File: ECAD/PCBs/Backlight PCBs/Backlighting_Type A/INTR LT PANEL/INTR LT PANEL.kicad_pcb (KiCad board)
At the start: 2 copper layers, 138.9 x 83.9 mm, 90 parts, among them J1 Conn_01x04_Female, J2 Conn_01x04_Female

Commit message: Drawing Sheet & Silkscreen update - Backlight Panels (Fc thru Spin)
1:  Updated/Relinked Drawing Sheet for both PCB and Schematics
2:  Standardized Silkscreen (if required)

Finished Remaining Backlighting Type A & Type B PCBs.....
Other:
- board text added: "INTR LT PANEL Revision: 3 www.openhornet.com"
- board text removed: "INTR LT PANEL Version 2.2 www.openhornet.com"
- board text removed: "Version 2.0"
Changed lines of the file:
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@@
   )
   (paper "A4")
+  (title_block
+    (title "INTR LT PANEL")
+    (date "2023-02-10")
+    (rev "3")
+  )
   (layers
     (0 "F.Cu" signal)
@@
     (effects (font (size 1 1) (thickness 0.15)) (justify mirror))
   )
-  (gr_text "INTR LT PANEL\nVersion 2.2\nwww.openhornet.com" (at 59.944 75.692) (layer "B.SilkS")
+  (gr_text "INTR LT PANEL\nRevision: 3\nwww.openhornet.com" (at 59.944 75.692) (layer "B.SilkS")
     (effects (font (size 1 1) (thickness 0.15)) (justify mirror))
   )
@@
     (effects (font (size 1 1) (thickness 0.15)) (justify mirror))
   )
-  (gr_text "Version 2.0" (at 157.375 81.55) (layer "B.SilkS")
-    (effects (font (size 1 1) (thickness 0.15)) (justify mirror))
-  )

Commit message: Review: HUD VID RCD thru INTR LT 100%
Reviewed/adjusted silkscreens as needed
Relinked footprints
Updated Manufacturing files
Updated PNGs and STEP files as needed.
Renamed PNGs for standardization
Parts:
- 1, 10, 11, 6: footprint OH_Backlighting:OH_Panel_6-32_PHS -> OH_Footprints:OH_Panel_6-32_PHS
- 2: footprint OH_Backlighting:SxAL_Toggle_13x13mm -> OH_Footprints:SxAL_Toggle_13x13mm
- 3, 4, 7, 8, 9: footprint OH_Backlighting:BR10K_Pot_11mm_x_11mm -> OH_Footprints:BR10K_Pot_11mm_x_11mm
- 5: footprint OH_Backlighting:631H_Toggle_13mm_x_13mm -> OH_Footprints:631H_Toggle_13mm_x_13mm
- G1: footprint Kicad Footprint Files:631HToggle -> OH_Footprints:631H_Toggle_Silkscreen; moved to F.Cu
- G2, G3, G4, G6, G7: footprint OH_Backlighting:BR10K_Pot_Silkscreen -> OH_Footprints:BR10K_Pot_Silkscreen; moved to F.Cu
- G5: footprint Kicad Footprint Files:S3ALToggle -> OH_Footprints:S3ALToggle
- G8: footprint OH_General:OH_LOGO_37.7mm_5.9mm -> OH_Footprints:OH_LOGO_37.7mm_5.9mm
- G9: footprint OH_General:CC-BY-NC-SA-Small -> OH_Footprints:CC-BY-NC-SA-Small
- moved G1 1.91 mm to (71.7, 106.9), turned to 0 degrees
- moved G7 0.74 mm to (100.7, 108.5), turned to 0 degrees
- turned G2 to 0 degrees
- turned G3 to 0 degrees
- turned G4 to 0 degrees
- turned G6 to 0 degrees

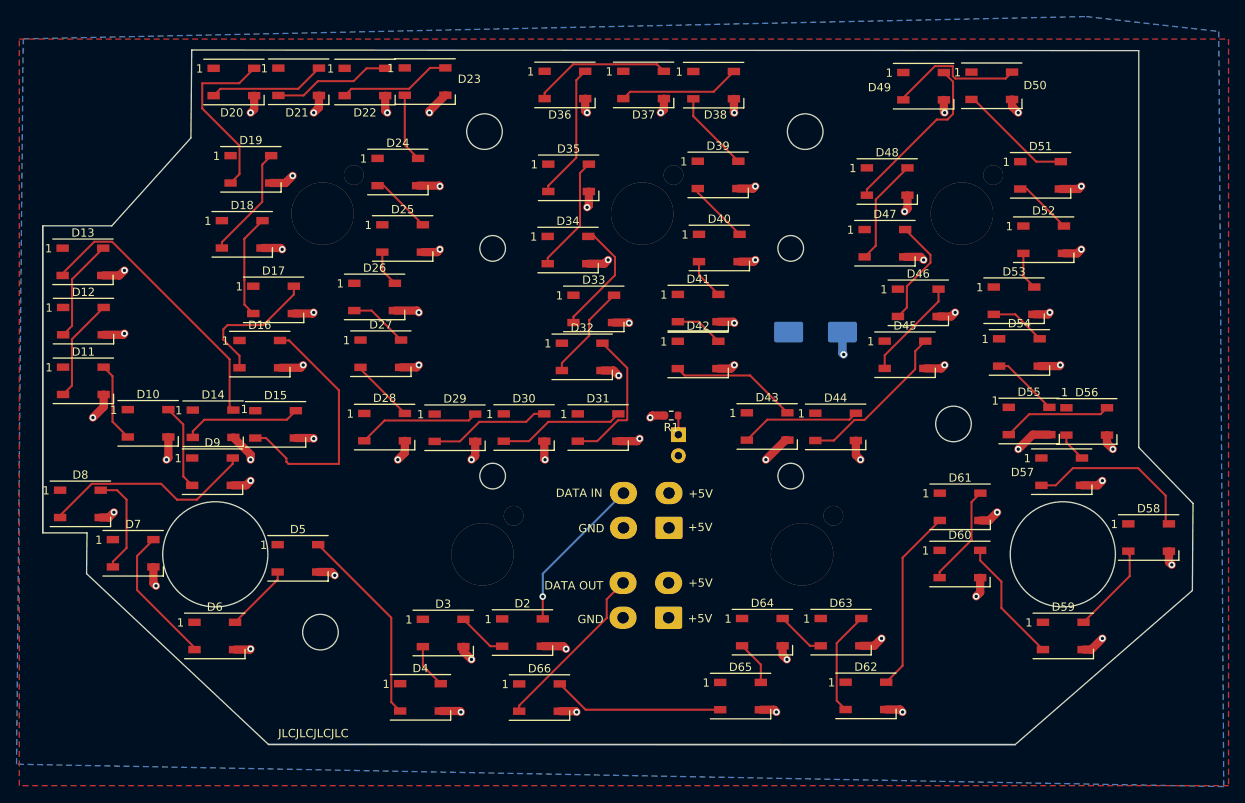
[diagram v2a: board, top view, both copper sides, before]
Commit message: KiCad 7 Transition - INTR LT Panel
PCB and Schematic standardization
Updated silkscreen text
Adjusted traces to prevent conflicts
Add Testpoints
Recompiled assets and manufacturing files
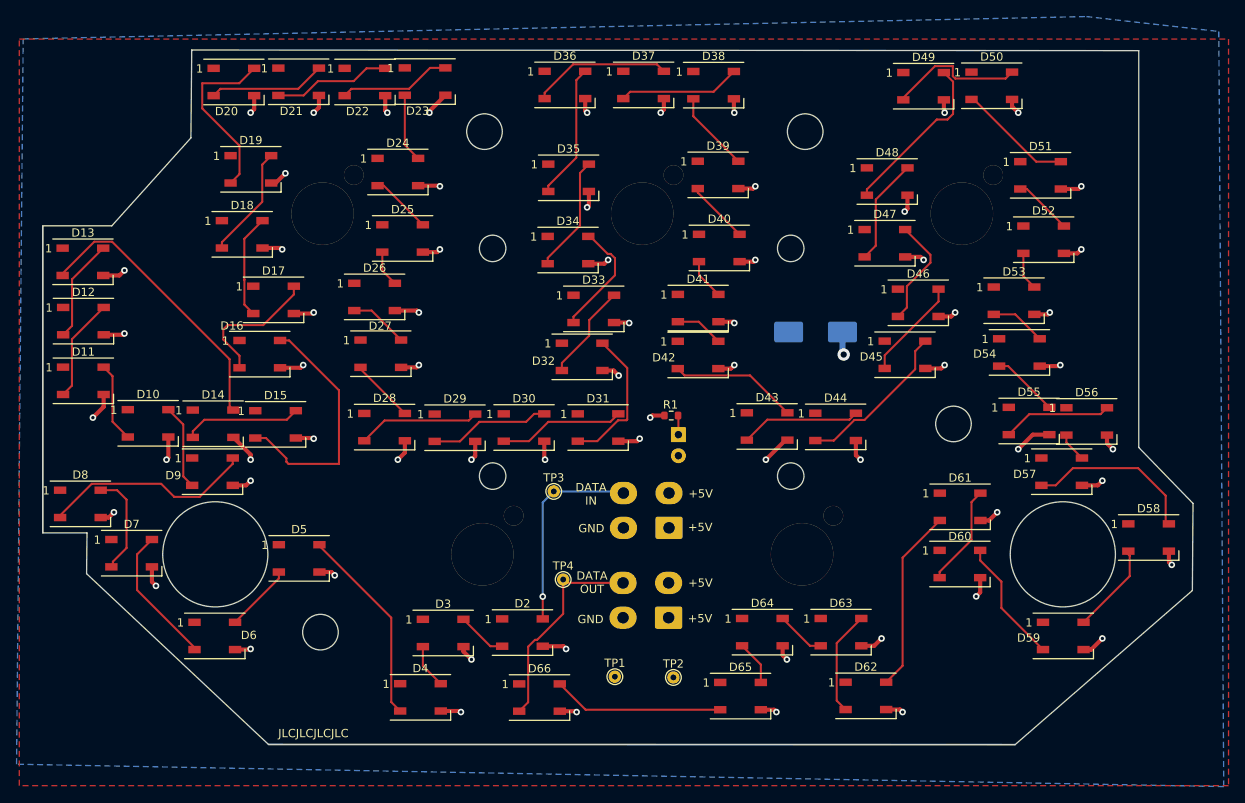
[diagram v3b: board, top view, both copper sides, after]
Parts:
- added MH5: M3 / 3.2mm, OH_Footprints:MountingHole_3.2mm_M3_DIN965, B.Cu at (94.0, 71.0)
- added MH6: M3 / 3.2mm, OH_Footprints:MountingHole_3.2mm_M3_DIN965, B.Cu at (130.0, 71.0)
- added MH7: M3 / 3.2mm, OH_Footprints:MountingHole_3.2mm_M3_DIN965, B.Cu at (94.0, 98.5)
- added MH8: M3 / 3.2mm, OH_Footprints:MountingHole_3.2mm_M3_DIN965, B.Cu at (130.0, 98.5)
- added TP1: TestPoint, OH_Footprints:TestPoint_THTPad_D1.5mm_Drill0.7mm, F.Cu at (108.8, 122.7)
- added TP2: TestPoint, OH_Footprints:TestPoint_THTPad_D1.5mm_Drill0.7mm, F.Cu at (115.8, 122.8)
- added TP3: TestPoint, OH_Footprints:TestPoint_THTPad_D1.5mm_Drill0.7mm, F.Cu at (101.4, 100.3)
- added TP4: TestPoint, OH_Footprints:TestPoint_THTPad_D1.5mm_Drill0.7mm, F.Cu at (102.5, 111.0)
- C1: value C_Polarized -> 1000uF
- D1: value LED -> Green
- J1, J2: value Conn_01x04_Female -> Mini-Fit Jr. 2x02
- LOGO1: renamed from G8; footprint OH_Footprints:OH_LOGO_37.7mm_5.9mm -> OH_Footprints:LOGO_OH_Text_Large
- LOGO2: renamed from G9; footprint OH_Footprints:CC-BY-NC-SA-Small -> OH_Footprints:LOGO_CC-BY-NC-SA_Half_Small
- LOGO3: renamed from G2; moved to B.Cu
- LOGO4: renamed from G3; moved to B.Cu
- LOGO5: renamed from G4; moved to B.Cu
- LOGO6: renamed from G1; footprint OH_Footprints:631H_Toggle_Silkscreen -> OH_Footprints:631H2_Toggle_Silkscreen; moved to B.Cu
- LOGO7: renamed from G7; moved to B.Cu
- LOGO8: renamed from G6; moved to B.Cu
- LOGO9: renamed from G5; footprint OH_Footprints:S3ALToggle -> OH_Footprints:S3AL_Toggle_Silkscreen
- MH1: renamed from 11; value OH_Panel_Fastner_Keepout -> 6x32 / 4mm; footprint OH_Footprints:OH_Panel_6-32_PHS -> OH_Footprints:MountingHole_6-32_PHS; moved to B.Cu
- MH10: renamed from 8; value BR10K_Pot_11mm_x_11mm -> Pot_B10K
- MH11: renamed from 7; value BR10K_Pot_11mm_x_11mm -> Pot_B10K
- MH12: renamed from 4; value BR10K_Pot_11mm_x_11mm -> Pot_B10K
- MH13: renamed from 3; value BR10K_Pot_11mm_x_11mm -> Pot_B10K
- MH14: renamed from 5; value 631H_Toggle_13mm_x_13mm -> Switch_631H; footprint OH_Footprints:631H_Toggle_13mm_x_13mm -> OH_Footprints:631HX_Toggle_13mm_x_13mm
- MH15: renamed from 2; value SxAL_Toggle_13x13mm -> Switch_631H; footprint OH_Footprints:SxAL_Toggle_13x13mm -> OH_Footprints:631HX_Toggle_13mm_x_13mm
- MH2: renamed from 10; value OH_Panel_Fastner_Keepout -> 6x32 / 4mm; footprint OH_Footprints:OH_Panel_6-32_PHS -> OH_Footprints:MountingHole_6-32_PHS; moved to B.Cu
- MH3: renamed from 6; value OH_Panel_Fastner_Keepout -> 6x32 / 4mm; footprint OH_Footprints:OH_Panel_6-32_PHS -> OH_Footprints:MountingHole_6-32_PHS; moved to B.Cu
- MH4: renamed from 1; value OH_Panel_Fastner_Keepout -> 6x32 / 4mm; footprint OH_Footprints:OH_Panel_6-32_PHS -> OH_Footprints:MountingHole_6-32_PHS; moved to B.Cu
- MH9: renamed from 9; value BR10K_Pot_11mm_x_11mm -> Pot_B10K
- R1: value R -> 470
- moved LOGO2 54.0 mm to (121.3, 47.4)
- moved LOGO8 1.72 mm to (138.7, 107.7), turned to 180 degrees
- moved LOGO7 0.96 mm to (99.8, 108.5), turned to 180 degrees
- moved LOGO9 0.64 mm to (172.5, 108.8)
- moved LOGO1 0.43 mm to (89.0, 81.3)
- moved D7 0.18 mm to (50.4, 107.8)
- moved D5 0.15 mm to (70.6, 108.4)
- turned LOGO3 to 180 degrees
- turned LOGO4 to 180 degrees
- turned LOGO5 to 180 degrees
- turned LOGO6 to 180 degrees
- turned MH1 to 180 degrees
- turned MH2 to 180 degrees
- turned MH3 to 180 degrees
- turned MH4 to 180 degrees
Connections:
- net /DATAIN renamed DATA IN
- net /DATAOUT renamed DATA OUT
- net /LED+5V renamed +5V
- net /LEDGND renamed GND
- net Net-(D14-Pad2) renamed /DATA1
- net Net-(D27-Pad2) renamed /DATA2
- net Net-(D40-Pad2) renamed /DATA3
- net Net-(D53-Pad2) renamed /DATA4
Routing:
- net DATA IN: track 19.2 -> 24.2 mm
- net DATA OUT: track 20.7 -> 25.1 mm
- net GND: track 157.9 -> 157.0 mm
- net Net-(D8-DOUT): track 26.0 -> 25.4 mm
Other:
- outline, holes or cut-outs redrawn
- board text added: "0.2000 mm / 0.0000 mm"
- board text added: "0.3000 mm"
- board text added: "1.6000 mm"
- board text added: "138.9126 mm x 83.8962 mm"
- board text added: "BOARD CHARACTERISTICS"
- board text added: "Board Thickness:"
- board text added: "Board overall dimensions:"
- board text added: "Castellated pads:"
- board text added: "Copper Finish:"
- board text added: "Copper Layer Count:"
- board text added: "Edge card connectors:"
- board text added: "INTR LT PANEL REV: 4 WWW.OPENHORNET.COM"
- board text added: "Impedance Control:"
- board text added: "Min hole diameter:"
- board text added: "Min track/spacing:"
- board text added: "No"
- board text added: "None"
- board text added: "POWER REQUIREMENTS: VOLTAGE: 5V DC LEDS: 65 CURRENT: 3.92A WATTAGE: 19.6W"
- board text added: "Plated Board Edge:"
- board text removed: "IN"
- board text removed: "INTR LT PANEL Revision: 3 www.openhornet.com"
- board text removed: "POWER REQUIREMENTS: VOLTAGE: 5V DC LEDS: 53 CURRENT: 3.18A WATTAGE: 15.9W"
- board text removed: "Switch PCB H1"
- board text removed: "Switch PCB H2"
- board text removed: "Switch PCB H3"
- board text removed: "Switch PCB H4"
- board text removed: "THRU"
- board text removed: "⌀3MM"
